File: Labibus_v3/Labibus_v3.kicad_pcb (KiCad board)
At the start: 2 copper layers, 40.5 x 42.9 mm, 43 parts, among them J1 Screw_Terminal_01x04, J2 Conn_01x16, J3 Conn_01x06, J4 Conn_01x03, J5 Conn_01x15, J6 Conn_01x12, J7 Conn_01x04 Qwiic JST SH 4-pin, SW1 SW_Push, U1 MIC5205-5.0YM5, U2 MAX485E, U3 ATmega328P-AU, U4 MIC5219-3.3YM5, Y1 Crystal_GND2_Small

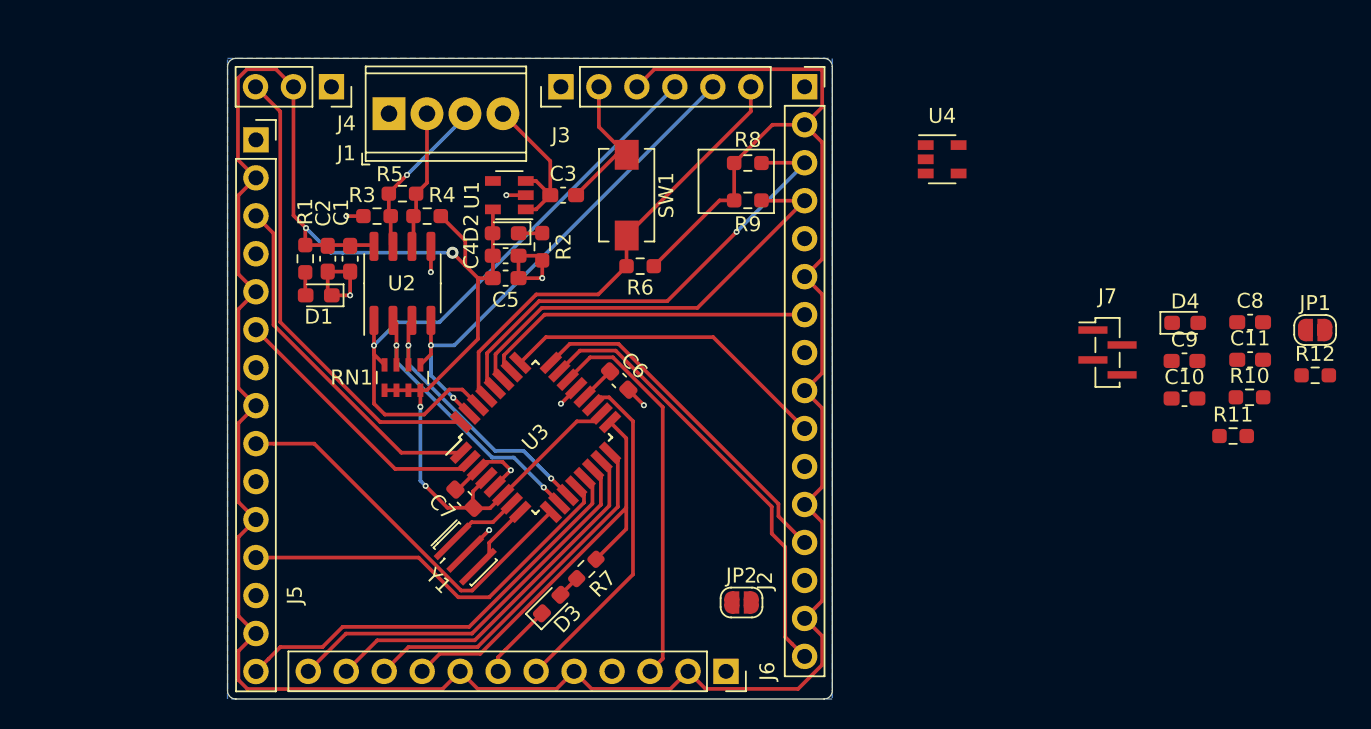
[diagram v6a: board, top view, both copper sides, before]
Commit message: update with: 3.3V and 5V select JST connector
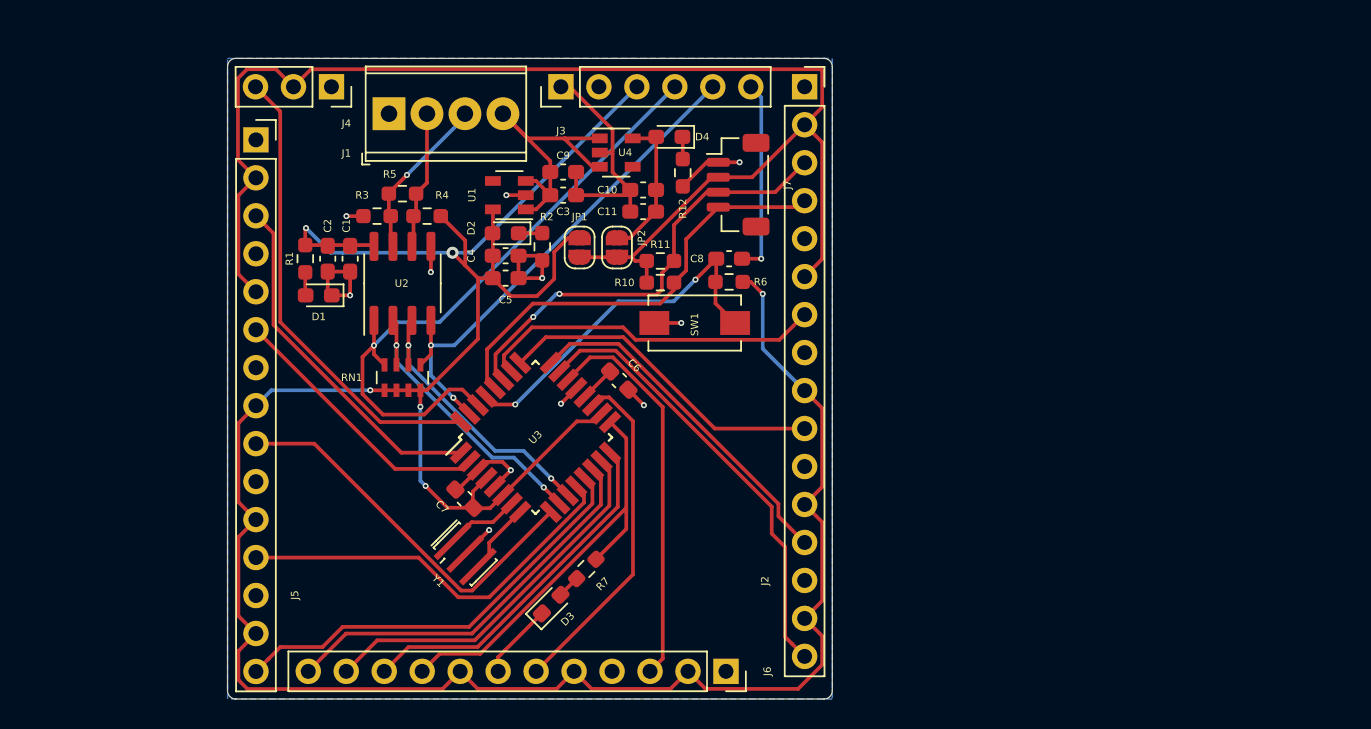
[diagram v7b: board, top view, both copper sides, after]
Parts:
- removed R8, R9: 10k, Resistor_SMD:R_0603_1608Metric_Pad0.98x0.95mm_HandSolder
- J7: footprint Connector_PinSocket_1.00mm:PinSocket_1x04_P1.00mm_Vertical_SMD_Pin1Left -> Connector_JST:JST_SH_BM04B-SRSS-TB_1x04-1MP_P1.00mm_Vertical
- moved JP1 49.5 mm to (95.8, 58.5), turned to 270 degrees
- moved R12 44.4 mm to (102.8, 53.5), turned to 270 degrees
- moved C9 43.4 mm to (94.8, 53.5)
- moved C11 41.8 mm to (100.1, 56.1), turned to 180 degrees
- moved R10 40.1 mm to (101.2, 60.9), turned to 180 degrees
- moved R11 40.1 mm to (101.2, 59.5), turned to 180 degrees
- moved C10 38.8 mm to (100.1, 54.7), turned to 180 degrees
- moved D4 36.7 mm to (101.8, 51.1), turned to 180 degrees
- moved C8 35.1 mm to (105.8, 59.3)
- moved J7 27.1 mm to (106.5, 54.4), turned to 270 degrees
- moved JP2 25.2 mm to (98.3, 58.5), turned to 270 degrees
- moved U4 21.8 mm to (98.3, 52.2)
- moved SW1 9.69 mm to (103.5, 63.6), turned to 0 degrees
- moved R6 6.04 mm to (105.8, 60.9)
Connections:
- J2 pad 2: +5V -> /JST_Power
- J2 pad 3: /A5-SCL -> /A4-SDA
- J2 pad 4: /A4-SDA -> /A5-SCL
- J2 pad 6: +5V -> /JST_Power
- J3 pad 2: Net-(J3-Pad2) -> GND
- J4 pad 2: +5V -> /JST_Power
- J5 pad 2: +5V -> /JST_Power
- J5 pad 5: +5V -> /JST_Power
- J7 pad 3: /SDA -> /A4-SDA
- J7 pad 4: /SCL -> /A5-SCL
- R10 pad 2: +3V3 -> /JST_Power
- R11 pad 2: +3V3 -> /JST_Power
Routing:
- net /JST_Power: track 0.00 -> 93.1 mm
- net +5V: track 239.3 -> 192.7 mm, vias 4 -> 6
- net /PC6-RESET: track 0.00 -> 24.5 mm, vias 0 -> 2
- net /DTR: track 30.9 -> 13.1 mm, vias 0 -> 1
- net GND: track 42.5 -> 55.8 mm, vias 9 -> 11
- net /RAW: track 10.8 -> 21.1 mm
- net +3V3: track 0.00 -> 9.96 mm
- net /A5-SCL: track 32.0 -> 29.7 mm, vias 1 -> 0
- net Net-(D4-Pad1): track 0.00 -> 1.50 mm
- net /ARDUINO_P_RX: track 42.8 -> 43.5 mm
- net /A3: track 22.5 -> 23.2 mm
- net /A4-SDA: track 29.8 -> 30.0 mm, vias 0 -> 2
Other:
- board text added: "5/3.3"
- board text removed: "Optional for I2C"
